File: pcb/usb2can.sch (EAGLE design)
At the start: 48 parts, among them CON1 USB_A_MALESMD, IC1 ADM3053M, IC2 LD1117S33

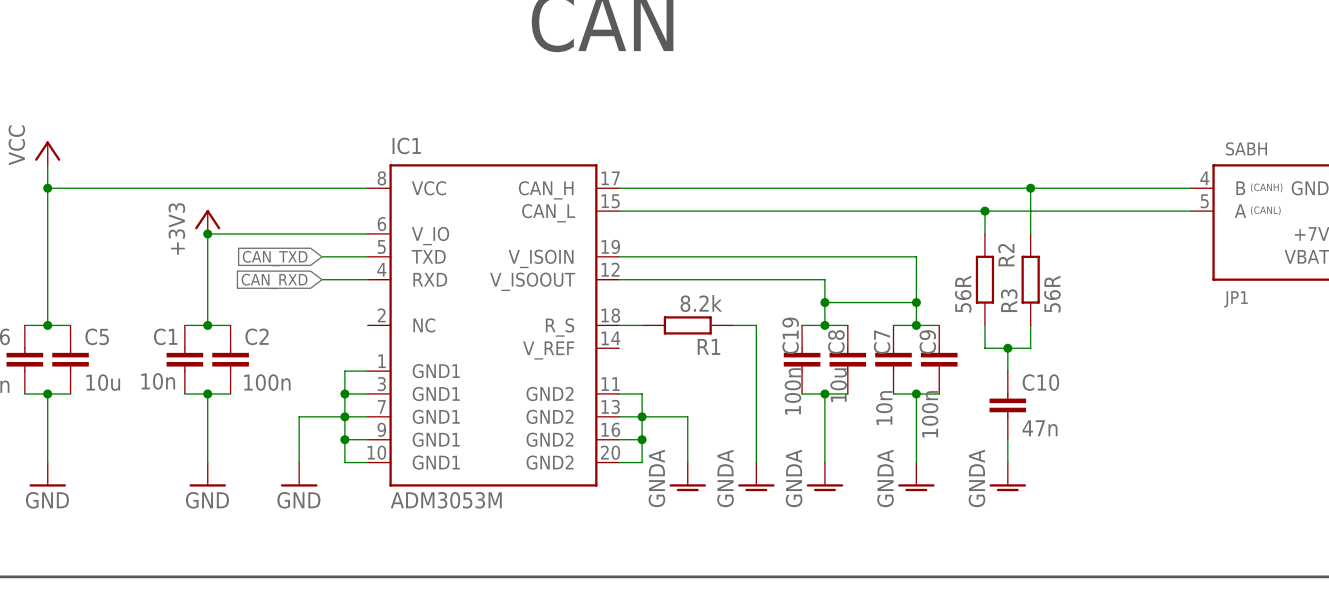
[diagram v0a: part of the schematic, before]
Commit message: schematic: Bypass Capacitors and Silk Screen
- Bypass capacitors: nearest capacitor should be the smallest.
- Add label to 100n capacitors
- Add label to LEDs
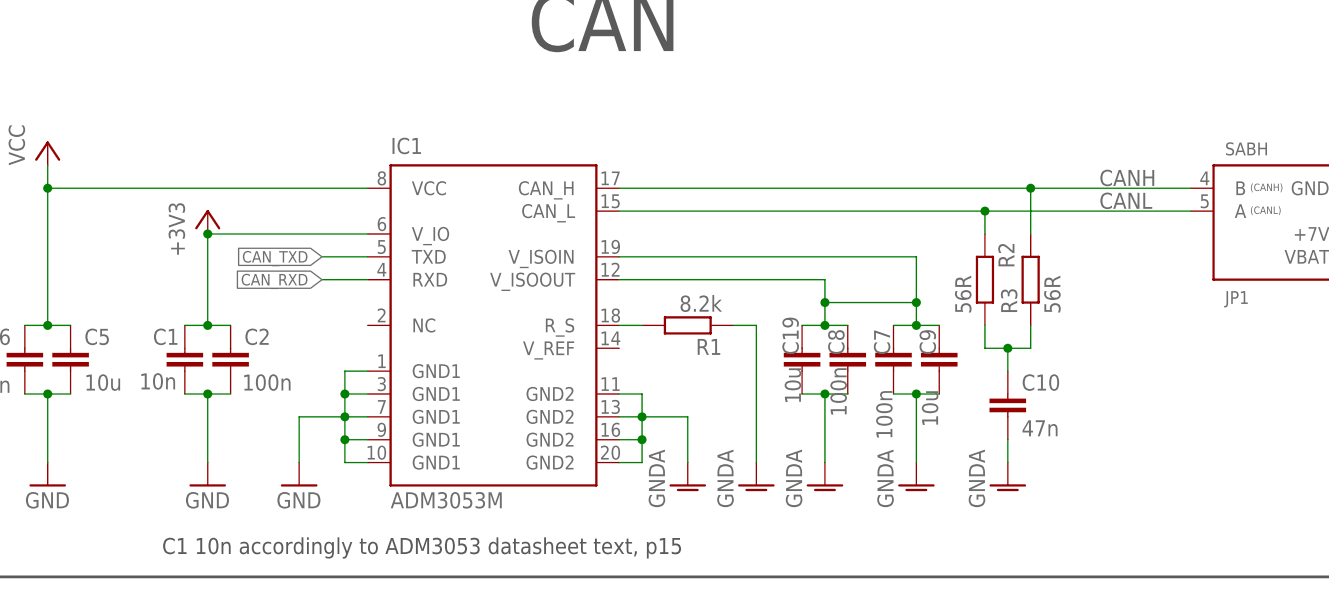
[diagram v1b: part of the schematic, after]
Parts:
- C19, C9: value 100n -> 10u
- C7: value 10n -> 100n
- C8: value 10u -> 100n
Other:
- note added: "C1 10n accordingly to ADM3053 datasheet text, p15"
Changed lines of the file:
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@@
 <part name="GND7" library="supply1" deviceset="GNDA" device=""/>
 <part name="GND8" library="supply1" deviceset="GNDA" device=""/>
-<part name="C9" library="rcl" deviceset="C-EU" device="C0805K" value="100n"/>
+<part name="C9" library="rcl" deviceset="C-EU" device="C0805K" value="10u"/>
 <part name="U$1" library="stm32" deviceset="STM32F072C" device="T"/>
 <part name="GND9" library="supply1" deviceset="GNDA" device=""/>
@@
 <part name="GND18" library="supply1" deviceset="GND" device=""/>
 <part name="CON1" library="micro_switch" deviceset="USB_A_MALE" device="SMD"/>
-<part name="C7" library="rcl" deviceset="C-EU" device="C0805K" value="10n"/>
-<part name="C8" library="rcl" deviceset="C-EU" device="C0805K" value="10u"/>
-<part name="C19" library="rcl" deviceset="C-EU" device="C0805K" value="100n"/>
+<part name="C7" library="rcl" deviceset="C-EU" device="C0805K" value="100n"/>
+<part name="C8" library="rcl" deviceset="C-EU" device="C0805K" value="100n"/>
+<part name="C19" library="rcl" deviceset="C-EU" device="C0805K" value="10u"/>
 <part name="GND19" library="supply1" deviceset="GNDA" device=""/>
 <part name="LED2" library="led" deviceset="LED" device="CHIPLED_0603" value="BLUE"/>
@@
 <text x="219.456" y="65.278" size="1.778" layer="97" ratio="12">Debug
 UART</text>
+<text x="68.58" y="-17.78" size="1.778" layer="97">C1 10n accordingly to ADM3053 datasheet text, p15</text>
 </plain>
 <instances>
@@
 <junction x="160.02" y="20.32"/>
 <pinref part="JP1" gate="G$1" pin="A"/>
+<label x="172.72" y="20.574" size="1.778" layer="95"/>
 </segment>
 </net>
@@
 <junction x="165.1" y="22.86"/>
 <pinref part="JP1" gate="G$1" pin="B"/>
-</segment>
-</net>
+<label x="172.72" y="23.114" size="1.778" layer="95"/>
+</segment>
+</net>

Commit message: schematic: Add text to buttons.
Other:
- note added: "DFU"
- note added: "MODE"
- note added: "RESET"
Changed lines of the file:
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@@
 UART</text>
 <text x="68.58" y="-17.78" size="1.778" layer="97">C1 10n accordingly to ADM3053 datasheet text, p15</text>
+<text x="121.92" y="71.12" size="1.778" layer="97">DFU</text>
+<text x="63.5" y="88.9" size="1.778" layer="97">RESET</text>
+<text x="236.22" y="53.34" size="1.778" layer="97">MODE</text>
 </plain>
 <instances>
